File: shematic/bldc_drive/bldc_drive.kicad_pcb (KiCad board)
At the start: 2 copper layers, 145 parts, among them IC1 TPS54140ADGQR, J1 Conn_01x04_Male, J2 Conn_01x04_Male, J3 Conn_01x04_Male, J4 Conn_01x02_Male, J5 Conn_01x02_Male, Q1 IRF1407, Q10 BC807, Q11 2N7002, Q12 2N7002, Q2 IRF1407, Q3 IRF1407, Q4 IRF1407, Q5 IRF1407, Q6 IRF1407, Q7 IRF1407, Q8 FDS6930B, Q9 BC817, U1 24LC08, U10 TJA1051T, U11 MAX481E, U12 SN74AUP1T34DCK, U13 SN74AUP1T34DCK, U14 uA7812, U15 AP1117-33, U2 STM32F042C6Tx, U3 A1302KUA-T, U4 A1302KUA-T, U5 A1302KUA-T, U6 IR2304, U7 IR2304, U8 IR2304, U9 INA193, Y1 Crystal

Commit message: --
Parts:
- removed C25: 100n, Capacitor_SMD:C_0603_1608Metric
- removed C26, C27, C28: C, Capacitor_SMD:C_0805_2012Metric
- removed C29: CP, Capacitor_SMD:C_Elec_8x6.2
- removed D11: B340, Diode_SMD:D_SMC
- removed H3, H4, H6: MountingHole_Pad, MountingHole:MountingHole_3.5mm_Pad_Via
- removed IC1: TPS54140ADGQR, msop10:SOP50P490X110-11N
- removed L3: INDUCTOR, Inductor_SMD:L_Bourns-SRN6028
- removed R38, R43, R44, R50, R51: R, Resistor_SMD:R_0603_1608Metric
- removed R49: R, Resistor_SMD:R_0805_2012Metric
- C23, C33: footprint Capacitor_THT:CP_Radial_D35.0mm_P10.00mm_SnapIn -> Capacitor_THT:CP_Radial_D18.0mm_P7.50mm
- C24: value C -> 1u; footprint Capacitor_SMD:C_0603_1608Metric -> Capacitor_SMD:C_1206_3216Metric
- L1, L2: footprint Inductor_THT:L_Axial_L30.0mm_D8.0mm_P35.56mm_Horizontal_Fastron_77A -> Inductor_THT:L_Axial_L20.0mm_D8.0mm_P25.40mm_Horizontal
- R27: footprint Resistor_SMD:R_2512_6332Metric -> Resistor_SMD:R_4020_10251Metric_Pad1.65x5.30mm_HandSolder
- U14: footprint Package_TO_SOT_THT:TO-220-3_Horizontal_TabDown -> Package_TO_SOT_THT:TO-220-3_Vertical
- U3, U4, U5: footprint Package_SIP:SIP3_11.6x8.5mm -> Package_TO_SOT_THT:TO-92_Wide
- U6, U7, U8: footprint Package_SO:SOIC-8-1EP_3.9x4.9mm_P1.27mm_EP2.29x3mm -> Package_SO:SO-8_3.9x4.9mm_P1.27mm
- moved H8 248.5 mm to (19.1, 171.4)
- moved H7 241.7 mm to (21.6, 143.5)
- moved U10 173.4 mm to (82.5, 162.6)
- moved U5 170.1 mm to (96.5, 172.7), turned to 195 degrees
- moved R6 167.5 mm to (97.0, 166.4)
- moved H5 165.9 mm to (53.3, 158.8)
- moved U3 165.1 mm to (113.2, 168.8), turned to 195 degrees
- moved U4 156.0 mm to (105.4, 171.4), turned to 195 degrees
- moved U15 141.6 mm to (124.5, 174.0)
- moved D1 129.7 mm to (122.3, 154.9)
- moved H2 126.0 mm to (74.8, 172.0)
- moved C24 124.8 mm to (82.5, 185.4)
- moved L2 124.7 mm to (53.2, 140.8), turned to 315 degrees
- moved H1 124.5 mm to (63.5, 166.4)
- moved J2 112.1 mm to (142.2, 151.1)
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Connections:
- H2 pad 1: Net-(C19-Pad1) -> Net-(C24-Pad1)
- J3 pad 2: Net-(J3-Pad2) -> (no net)
- R36 pad 2: ANALOG_IN -> (no net)
- R39 pad 2: IN_DISC_1 -> (no net)
- R41 pad 2: IN_DISC_2 -> (no net)
- U10 pad 5: Net-(U10-Pad5) -> (no net)
- U2 pad 3: Net-(U2-Pad3) -> (no net)
- U2 pad 4: Net-(U2-Pad4) -> (no net)
- U2 pad 40: Net-(U2-Pad40) -> (no net)
- U2 pad 41: Net-(U2-Pad41) -> (no net)
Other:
- board outline added: 106 x 65 mm

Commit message: 29.08.20
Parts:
- removed C3, C6: 15p, Capacitor_SMD:C_0603_1608Metric
- removed H7, H8: MountingHole_Pad, MountingHole:MountingHole_3.5mm_Pad_Via
- removed Y1: Crystal, Crystal:Crystal_HC49-4H_Vertical
- added H3: MountingHole_Pad, user_pads:MountingHole_6x2, F.Cu at (105.4, 124.5)
- added H4: MountingHole_Pad, user_pads:MountingHole_6x2, F.Cu at (74.9, 137.2)
- added H6: MountingHole_Pad, user_pads:MountingHole_6x2, F.Cu at (110.5, 143.5)
- added R38: 10k, Resistor_SMD:R_0603_1608Metric, F.Cu at (117.1, 145.5)
- added R43: 10k, Resistor_SMD:R_0603_1608Metric, F.Cu at (115.6, 145.5)
- added Y2: Crystal_GND2_Small, Crystal:Resonator_SMD_muRata_CSTxExxV-3Pin_3.0x1.1mm, F.Cu at (128.8, 167.6)
- C12: footprint Capacitor_SMD:C_Elec_8x6.2 -> Capacitor_SMD:C_1206_3216Metric
- J1: footprint Connector_PinHeader_2.54mm:PinHeader_1x04_P2.54mm_Vertical -> Connector_PinHeader_1.00mm:PinHeader_1x04_P1.00mm_Vertical
- J2: footprint Connector_PinHeader_2.54mm:PinHeader_1x04_P2.54mm_Vertical -> Connector_PinHeader_1.27mm:PinHeader_1x04_P1.27mm_Vertical
- U11: footprint Package_SO:SOIC-8-1EP_3.9x4.9mm_P1.27mm_EP2.29x3mm -> Package_SO:SOIC-8_3.9x4.9mm_P1.27mm
- moved C19 181.8 mm to (48.5, 168.8), turned to 90 degrees
- moved R7 178.0 mm to (91.4, 169.6), turned to 270 degrees
- moved R5 175.5 mm to (106.7, 168.4), turned to 270 degrees
- moved C32 175.3 mm to (111.3, 189.2)
- moved R1 159.2 mm to (127.0, 164.3), turned to 270 degrees
- moved J1 154.8 mm to (121.2, 150.6), turned to 90 degrees
- moved C4 152.9 mm to (134.4, 166.2), turned to 90 degrees
- moved U13 151.0 mm to (166.1, 179.8)
- moved R3 150.0 mm to (131.6, 164.3), turned to 90 degrees
- moved C1 147.9 mm to (130.0, 164.3), turned to 90 degrees
- moved C7 146.4 mm to (121.2, 148.8)
- moved R2 146.3 mm to (128.5, 164.3), turned to 90 degrees
- moved C8 146.1 mm to (125.0, 164.2), turned to 90 degrees
- moved R4 144.7 mm to (118.6, 145.5), turned to 90 degrees
- moved C22 143.9 mm to (97.4, 157.2)
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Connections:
- J4 pad 2: /interfaces/CAN_RES_SW -> CAN_L
- J5 pad 2: /interfaces/RS485_TERM -> RS485_A
- R32 pad 1: /interfaces/CAN_RES_SW -> CAN_H
- R33 pad 1: /interfaces/RS485_TERM -> RS485_B
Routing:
- net +V_POW: track 0.00 -> 113.3 mm
- net GND: track 0.00 -> 111.3 mm, vias 0 -> 1
- net LOCK_H: track 0.00 -> 88.1 mm, vias 0 -> 2
- net +12V: track 0.00 -> 87.0 mm, vias 0 -> 2
- net /cpu_io/HAL_C: track 0.00 -> 80.0 mm, vias 0 -> 1
- net /cpu_io/HAL_B: track 0.00 -> 68.6 mm, vias 0 -> 1
- net /FET_drive/AH: track 0.00 -> 67.2 mm
- net /cpu_io/HAL_A: track 0.00 -> 61.4 mm, vias 0 -> 1
- net +3V3: track 0.00 -> 55.5 mm
- net /FET_drive/AL: track 0.00 -> 52.8 mm
- net CURRENT_SENSE: track 0.00 -> 49.9 mm, vias 0 -> 2
- net /FET_drive/BH: track 0.00 -> 49.1 mm
- net Net-(C19-Pad1): track 0.00 -> 35.9 mm
- net /cpu_io/E_WP: track 0.00 -> 24.7 mm, vias 0 -> 3
- net /FET_drive/BL: track 0.00 -> 24.6 mm
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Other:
- outline, holes or cut-outs redrawn

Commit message: --
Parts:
- removed C14, C15: 1u, Capacitor_SMD:C_0805_2012Metric
- removed C16, C17, C18: 100n, Capacitor_SMD:C_0603_1608Metric
- removed C32: CP, Capacitor_SMD:C_Elec_8x5.4
- removed D12, D13, D8: DZ2S033X0L, Diode_SMD:D_SOD-523
- removed D6: 1N4148W, Diode_SMD:D_SOD-123
- removed Q11, Q12: 2N7002, Package_TO_SOT_SMD:SOT-23
- removed Q8: FDS6930B, Package_SO:SOIC-8_3.9x4.9mm_P1.27mm
- removed R34: R, Resistor_SMD:R_0603_1608Metric
- removed R36: 4k7, Resistor_SMD:R_0603_1608Metric
- removed R37: 2k2, Resistor_SMD:R_0603_1608Metric
- removed R39, R40, R41, R42: 10k, Resistor_SMD:R_0603_1608Metric
- removed U12, U13: SN74AUP1T34DCK, Package_TO_SOT_SMD:SOT-353_SC-70-5
- H2: footprint MountingHole:MountingHole_3.5mm_Pad_Via -> MountingHole:MountingHole_4.3mm_M4_Pad_Via
- L1, L2: footprint Inductor_THT:L_Axial_L20.0mm_D8.0mm_P25.40mm_Horizontal -> Inductor_THT:L_Axial_L16.0mm_D6.3mm_P20.32mm_Horizontal_Fastron_VHBCC
- moved R45 55.2 mm to (119.9, 172.2)
- moved D10 47.5 mm to (116.2, 173.5)
- moved D9 47.4 mm to (116.2, 171.4), turned to 180 degrees
- moved J2 43.7 mm to (104.6, 160.3), turned to 270 degrees
- moved C20 40.0 mm to (120.4, 175.6), turned to 270 degrees
- moved D16 36.5 mm to (125.2, 175.8), turned to 270 degrees
- moved R47 35.5 mm to (121.7, 172.2), turned to 90 degrees
- moved R46 16.9 mm to (122.2, 175.7), turned to 90 degrees
- moved C21 16.0 mm to (129.0, 175.7), turned to 270 degrees
- moved R48 15.2 mm to (127.0, 175.7), turned to 90 degrees
- moved D14 14.3 mm to (123.7, 175.8), turned to 270 degrees
- moved L1 3.01 mm to (70.0, 153.8)
- moved L2 2.41 mm to (44.5, 145.5)
- moved H4 2.05 mm to (75.2, 135.1), turned to 80 degrees
- moved C33 1.84 mm to (56.8, 141.5)
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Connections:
- H3 pad 1: /FET_drive/PA -> /FET_drive/PB
- H4 pad 1: /FET_drive/PB -> /FET_drive/PA
- J2 pad 1: ext_TX -> U2TX
- J2 pad 2: ext_RX -> U2RX
- J2 pad 3: /interfaces/ext_3v3 -> GND
- U2 pad 17: V_ANALOG_IO -> (no net)
- U2 pad 21: DISC_IN_1 -> (no net)
- U2 pad 22: DISC_IN_2 -> (no net)
- U2 pad 38: OD_OUT_1_MCU -> (no net)
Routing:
- net GND: track 111.3 -> 483.9 mm, vias 1 -> 11
- net +3V3: track 55.5 -> 198.2 mm, vias 0 -> 9
- net Net-(Q1-Pad2): track 10.6 -> 132.5 mm, vias 0 -> 4
- net +12V: track 87.0 -> 191.1 mm, vias 2 -> 4
- net /FET_drive/PA: track 6.22 -> 96.4 mm, vias 0 -> 1
- net Net-(Q2-Pad3): track 0.00 -> 82.1 mm
- net /FET_drive/PC: track 6.48 -> 76.7 mm, vias 0 -> 1
- net U2TX: track 0.00 -> 54.9 mm, vias 0 -> 2
- net U2RX: track 0.00 -> 52.4 mm, vias 0 -> 1
- net /FET_drive/PB: track 6.53 -> 58.1 mm, vias 0 -> 3
- net V_POW_MEAS: track 6.48 -> 57.8 mm, vias 0 -> 2
- net Vin: track 0.00 -> 39.1 mm, vias 0 -> 2
- net Vin_ref: track 0.00 -> 32.4 mm, vias 0 -> 2
- net Net-(D10-Pad2): track 0.00 -> 29.1 mm
- net /FET_drive/AH: track 67.2 -> 81.1 mm
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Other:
- outline, holes or cut-outs redrawn

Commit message: 30.08.20
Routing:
- net GND: track 483.9 -> 485.2 mm
- net /cpu_io/HAL_A: track 61.4 -> 62.4 mm
- net /cpu_io/HAL_C: track 80.0 -> 80.7 mm
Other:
- board text added: "BLDC Motor driver powered by Ivan Bobovich"

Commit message: --
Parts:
- added REF**: KiCad-Logo2_6mm_SilkScreen, Symbol:KiCad-Logo2_6mm_SilkScreen, F.Cu at (95.8, 133.6)
- C10, C11, C9: footprint Capacitor_Tantalum_SMD:CP_EIA-6032-28_Kemet-C -> Capacitor_SMD:C_1206_3216Metric
- C2: footprint Capacitor_SMD:C_0805_2012Metric -> Capacitor_SMD:C_0603_1608Metric
- C3: renamed from C4; footprint Capacitor_SMD:C_0805_2012Metric -> Capacitor_SMD:C_0603_1608Metric
- C4: renamed from C5; footprint Capacitor_SMD:C_0805_2012Metric -> Capacitor_SMD:C_0603_1608Metric
- C5: renamed from C7; footprint Capacitor_SMD:C_0805_2012Metric -> Capacitor_SMD:C_0603_1608Metric
- C6: renamed from C8; footprint Capacitor_SMD:C_0805_2012Metric -> Capacitor_SMD:C_0603_1608Metric
- R23: renamed from R20; footprint Resistor_SMD:R_0805_2012Metric -> Resistor_SMD:R_0603_1608Metric
- moved R7 4.05 mm to (106.7, 164.4)
- moved D10 2.81 mm to (116.0, 176.3)
- moved D9 1.92 mm to (116.0, 173.4)
- moved R8 0.97 mm to (100.3, 168.7)
- moved D11 0.63 mm to (119.1, 167.1)
- moved J3 0.63 mm to (144.3, 156.8)
- moved D7 0.57 mm to (123.7, 176.3)
- moved C9 0.55 mm to (120.8, 129.5)
- moved C7 0.54 mm to (143.6, 144.7)
- moved D8 0.51 mm to (125.2, 176.3)
- moved J4 0.51 mm to (144.3, 160.5)
- moved R38 0.40 mm to (122.0, 176.1)
- moved C12 0.40 mm to (120.3, 176.0)
- moved R40 0.38 mm to (127.0, 176.1)
- moved C13 0.28 mm to (128.9, 175.9)
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- renumbered C20 to C12, C21 to C13, C22 to C14, C19 to C15, C33 to C16, C23 to C17, C24 to C18, C30 to C19, C31 to C20, C12 to C7, C13 to C8, D15 to D11, D5 to D2, D2 to D3, D3 to D4, D4 to D5, D7 to D6, D14 to D7, D16 to D8, H4 to H1, H3 to H2, H6 to H3, H1 to H4, H2 to H6, J4 to J3, J5 to J4, J3 to J5, Q9 to Q1, Q10 to Q2, Q1 to Q3, Q2 to Q4, Q3 to Q5, Q4 to Q6, Q5 to Q7, Q6 to Q8, Q7 to Q9, R8 to R10, R9 to R11, R10 to R12, R11 to R13, R12 to R14, R13 to R15, R14 to R16, R15 to R17, R35 to R18, R16 to R19, R17 to R20, R18 to R21, R19 to R22, R21 to R24, R22 to R25, R23 to R26, R24 to R27, R25 to R28, R26 to R29, R27 to R30, R28 to R31, R29 to R32, R30 to R33, R31 to R34, R32 to R35, R33 to R36, R45 to R37, R46 to R38, R47 to R39, R38 to R4, R48 to R40, R43 to R5, R4 to R6, R5 to R7, R6 to R8, R7 to R9, U14 to U12, U15 to U13, Y2 to Y1
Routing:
- net /cpu_io/HAL_A: track 62.4 -> 67.2 mm, vias 1 -> 2
- net Net-(D10-Pad2): track 29.1 -> 25.1 mm
- net GND: track 485.2 -> 488.9 mm, vias 11 -> 12
- net Vin_ref: track 32.4 -> 35.9 mm
- net Net-(D10-Pad1): track 6.25 -> 9.55 mm
- net +12V: track 191.1 -> 193.1 mm
- net +3V3: track 198.2 -> 200.0 mm
- net CAN_H: track 15.0 -> 16.4 mm
- net /FET_drive/PC: track 76.7 -> 77.9 mm
- net /FET_drive/PB: track 58.1 -> 59.2 mm
- net CAN_L: track 8.52 -> 9.60 mm
- net Net-(C11-Pad1): track 10.6 -> 11.7 mm
- net Net-(C10-Pad1): track 9.97 -> 11.0 mm
- net /cpu_io/HAL_B: track 68.6 -> 69.6 mm
- net /FET_drive/PA: track 96.4 -> 95.6 mm
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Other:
- net class Default: clearance 0.2 -> 0.15
- rule trace_clearance: 0.2 -> 0.15

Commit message: --
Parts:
- U1, U6, U7, U8: footprint Package_SO:SO-8_3.9x4.9mm_P1.27mm -> Package_SO:SOIC-8_3.9x4.9mm_P1.27mm
- moved REF** 76.1 mm to (110.0, 58.8)
- moved C16 75.8 mm to (71.4, 67.1)
- moved C18 75.8 mm to (96.8, 99.6)
- moved C3 75.8 mm to (149.0, 91.8)
- moved C4 75.8 mm to (130.2, 73.9)
- moved C8 75.8 mm to (113.2, 70.9)
- moved D1 75.8 mm to (137.3, 89.8)
- moved D10 75.8 mm to (130.6, 101.9)
- moved D2 75.8 mm to (110.3, 70.8)
- moved H3 75.8 mm to (124.6, 69.3)
- moved H4 75.8 mm to (70.5, 95.8)
- moved J1 75.8 mm to (135.8, 76.2)
- moved J5 75.8 mm to (138.9, 97.7)
- moved R23 75.8 mm to (109.1, 66.5)
- moved R30 75.8 mm to (99.2, 68.6)
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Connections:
- J5 pad 2: (no net) -> Net-(J5-Pad2)
- U10 pad 5: (no net) -> Net-(U10-Pad5)
- U2 pad 17: (no net) -> V_ANALOG_IO
- U2 pad 21: (no net) -> DISC_IN_1
- U2 pad 22: (no net) -> DISC_IN_2
- U2 pad 3: (no net) -> Net-(U2-Pad3)
- U2 pad 38: (no net) -> OD_OUT_1_MCU
- U2 pad 4: (no net) -> Net-(U2-Pad4)
- U2 pad 40: (no net) -> Net-(U2-Pad40)
- U2 pad 41: (no net) -> Net-(U2-Pad41)
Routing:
- net GND: track 488.9 -> 518.0 mm, vias 12 -> 13
- net /FET_drive/PA: track 95.6 -> 97.5 mm
- net +12V: track 193.1 -> 194.7 mm
- net +V_POW: track 103.6 -> 104.5 mm
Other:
- outline, holes or cut-outs redrawn
- board text added: "BLDC Motor driver make on Ivan B. Labs"
- board text removed: "BLDC Motor driver powered by Ivan Bobovich"

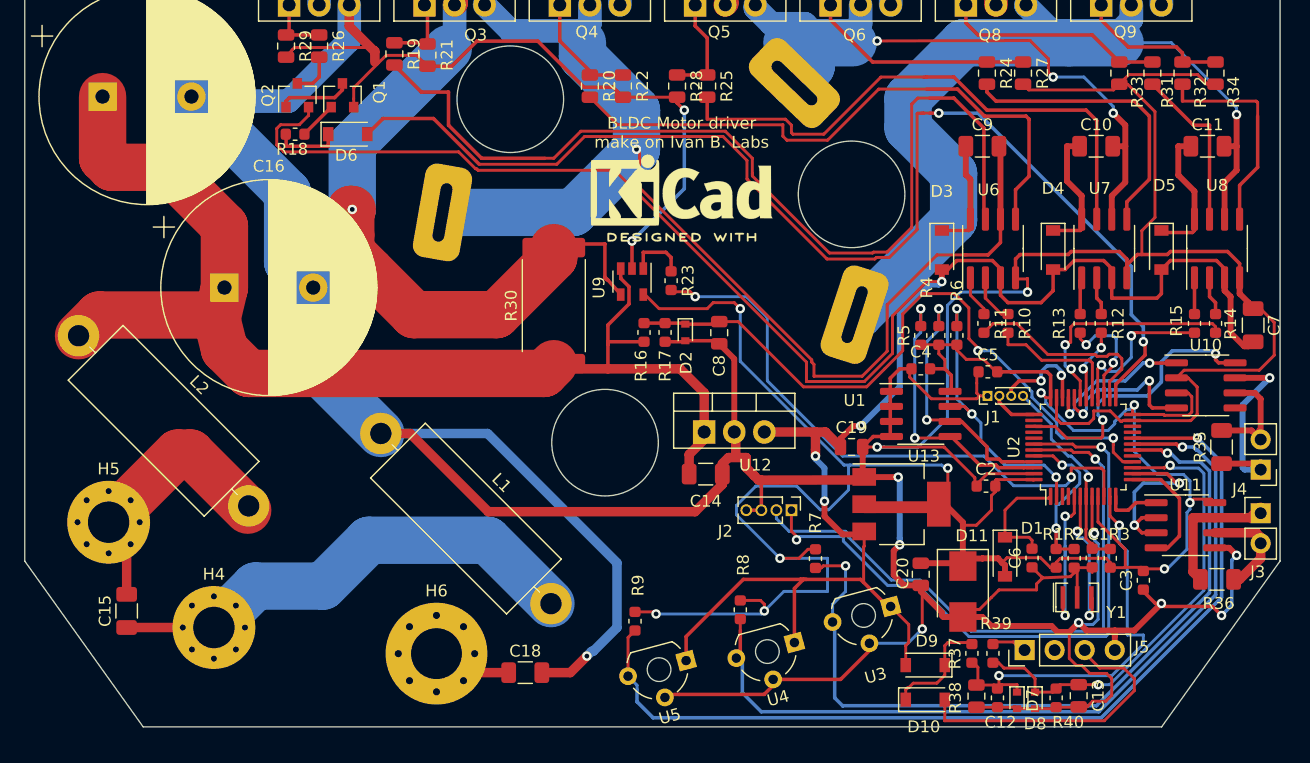
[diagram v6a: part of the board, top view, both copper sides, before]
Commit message: replace ir2304 to ir2101
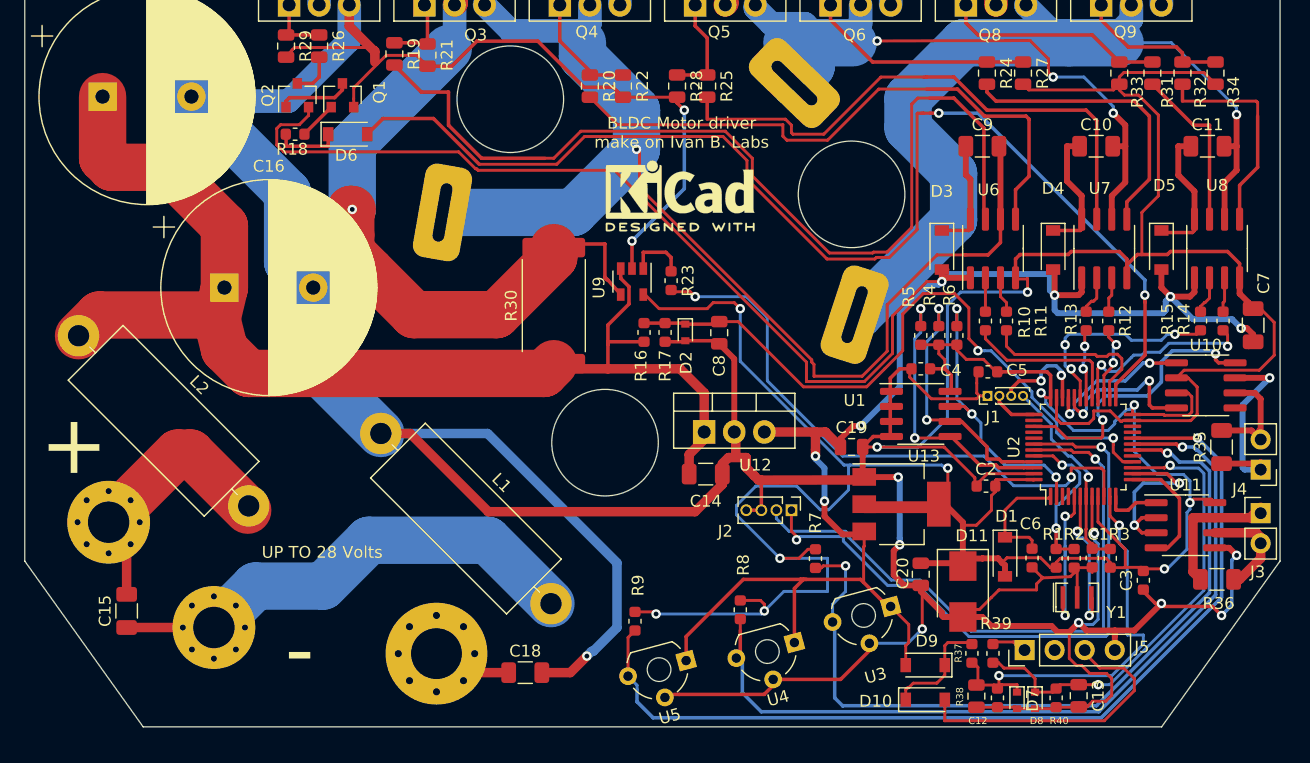
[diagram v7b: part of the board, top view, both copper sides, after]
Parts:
- removed the REF** at (110.0, 58.8)
- added REF**: KiCad-Logo2_5mm_SilkScreen, Symbol:KiCad-Logo2_5mm_SilkScreen, F.Cu at (109.9, 59.3)
- U6, U7, U8: value IR2304 -> IR2101
- moved R13 2.42 mm to (146.1, 69.9)
- moved R15 2.42 mm to (155.7, 69.9)
- moved R10 1.92 mm to (135.6, 69.9)
- moved R11 1.92 mm to (137.4, 69.9)
- moved R14 1.29 mm to (153.8, 69.9)
- moved R12 1.29 mm to (144.1, 69.9)
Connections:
- J5 pad 2: Net-(J5-Pad2) -> (no net)
- U10 pad 5: Net-(U10-Pad5) -> (no net)
- U2 pad 17: V_ANALOG_IO -> (no net)
- U2 pad 21: DISC_IN_1 -> (no net)
- U2 pad 22: DISC_IN_2 -> (no net)
- U2 pad 3: Net-(U2-Pad3) -> (no net)
- U2 pad 38: OD_OUT_1_MCU -> (no net)
- U2 pad 4: Net-(U2-Pad4) -> (no net)
- U2 pad 40: Net-(U2-Pad40) -> (no net)
- U2 pad 41: Net-(U2-Pad41) -> (no net)
- U6 pad 1: Net-(R11-Pad1) -> +12V
- U6 pad 3: +12V -> Net-(R11-Pad1)
- U7 pad 1: Net-(R13-Pad1) -> +12V
- U7 pad 3: +12V -> Net-(R13-Pad1)
- U8 pad 1: Net-(R15-Pad1) -> +12V
- U8 pad 3: +12V -> Net-(R15-Pad1)
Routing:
- net +12V: track 194.7 -> 199.6 mm, vias 4 -> 7
- net LCL: track 13.5 -> 16.5 mm
- net LBL: track 10.4 -> 7.48 mm
- net LCH: track 19.9 -> 17.8 mm, vias 2 -> 3
- net LAH: track 11.9 -> 13.5 mm
- net LAL: track 17.1 -> 15.4 mm
- net Net-(R10-Pad1): track 4.08 -> 2.86 mm
- net GND: track 518.0 -> 519.0 mm
- net Net-(R15-Pad1): track 2.96 -> 3.79 mm
- net Net-(R13-Pad1): track 3.01 -> 3.84 mm
- net Net-(R11-Pad1): track 3.44 -> 3.94 mm
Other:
- board text added: "+"
- board text added: "-"
- board text added: "UP TO 28 Volts"
